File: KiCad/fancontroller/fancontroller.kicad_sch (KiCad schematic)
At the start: 17 parts, among them IC1 NE555DR, IC2 LM311DR, IC3 NE555DR, J1 Fan 4-pin, J2 Power input, P1 10k

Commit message: feat: save PCB reconstruction checkpoint and detailed passdown
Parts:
- added H1, H2, H3, H4: M2 mounting hole, MountingHole:MountingHole_2.2mm_M2, symbol Mechanical:MountingHole
- J1: footprint (none) -> Connector:FanPinHeader_1x04_P2.54mm_Vertical
- J2: footprint (none) -> Connector_PinHeader_2.54mm:PinHeader_1x02_P2.54mm_Vertical
- P1: footprint (none) -> Connector_PinHeader_2.54mm:PinHeader_1x03_P2.54mm_Vertical
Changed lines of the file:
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@@
 			(effects (font (size 1.27 1.27)))
 		)
-		(property "Footprint" ""
+		(property "Footprint" "Connector_PinHeader_2.54mm:PinHeader_1x03_P2.54mm_Vertical"
 			(at 124.46 100.33 0)
 			(effects (font (size 1.27 1.27)) (hide yes))
@@
 			(effects (font (size 1.27 1.27)))
 		)
-		(property "Footprint" ""
+		(property "Footprint" "Connector:FanPinHeader_1x04_P2.54mm_Vertical"
 			(at 265.43 64.77 0)
 			(effects (font (size 1.27 1.27)) (hide yes))
@@
 			(effects (font (size 1.27 1.27)))
 		)
-		(property "Footprint" ""
+		(property "Footprint" "Connector_PinHeader_2.54mm:PinHeader_1x02_P2.54mm_Vertical"
 			(at 265.43 115.57 0)
 			(effects (font (size 1.27 1.27)) (hide yes))
@@
 	(no_connect (at 144.78 77.47))
 	(no_connect (at 147.32 77.47))
+	(symbol
+		(lib_id "Mechanical:MountingHole")
+		(at 30.48 30.48 0)
+		(unit 1)
+		(exclude_from_sim no)
+		(in_bom yes)
+		(on_board yes)
+		(dnp no)
+		(property "Reference" "H1"
+			(at 30.48 26.67 0)
+			(effects (font (size 1.27 1.27)))
+		)
+		(property "Value" "M2 mounting hole"
+			(at 30.48 34.29 0)
+			(effects (font (size 1.27 1.27)))
+		)
+		(property "Footprint" "MountingHole:MountingHole_2.2mm_M2"
+			(at 30.48 30.48 0)
+			(effects (font (size 1.27 1.27)) (hide yes))
+		)
+		(property "Datasheet" "~"
+			(at 30.48 30.48 0)
+			(effects (font (size 1.27 1.27)) (hide yes))
+		)
+		(instances
+			(project "fancontroller"
+				(path "/97550efb-8a25-4e8f-a675-896628ec4139"
+					(reference "H1") (unit 1)
+				)
+			)
+		)
+	)
+	(symbol
+		(lib_id "Mechanical:MountingHole")
+		(at 50.8 30.48 0)
+		(unit 1)
+		(exclude_from_sim no)
+		(in_bom yes)
+		(on_board yes)
+		(dnp no)
+		(property "Reference" "H2"
+			(at 50.8 26.67 0)
+			(effects (font (size 1.27 1.27)))
+		)
+		(property "Value" "M2 mounting hole"
+			(at 50.8 34.29 0)
+			(effects (font (size 1.27 1.27)))
+		)
+		(property "Footprint" "MountingHole:MountingHole_2.2mm_M2"
+			(at 50.8 30.48 0)
+			(effects (font (size 1.27 1.27)) (hide yes))
+		)
+		(property "Datasheet" "~"
+			(at 50.8 30.48 0)
+			(effects (font (size 1.27 1.27)) (hide yes))
+		)
+		(instances
+			(project "fancontroller"
+				(path "/97550efb-8a25-4e8f-a675-896628ec4139"
+					(reference "H2") (unit 1)
+				)
+			)
+		)
+	)
+	(symbol
+		(lib_id "Mechanical:MountingHole")
+		(at 175.26 30.48 0)
+		(unit 1)
+		(exclude_from_sim no)
+		(in_bom yes)
+		(on_board yes)
+		(dnp no)
+		(property "Reference" "H3"
+			(at 175.26 26.67 0)
+			(effects (font (size 1.27 1.27)))
+		)
+		(property "Value" "M2 mounting hole"
+			(at 175.26 34.29 0)
+			(effects (font (size 1.27 1.27)))
+		)
+		(property "Footprint" "MountingHole:MountingHole_2.2mm_M2"
+			(at 175.26 30.48 0)
+			(effects (font (size 1.27 1.27)) (hide yes))
+		)
+		(property "Datasheet" "~"
+			(at 175.26 30.48 0)
+			(effects (font (size 1.27 1.27)) (hide yes))
+		)
+		(instances
+			(project "fancontroller"
+				(path "/97550efb-8a25-4e8f-a675-896628ec4139"
+					(reference "H3") (unit 1)
+				)
+			)
+		)
+	)
+	(symbol
+		(lib_id "Mechanical:MountingHole")
+		(at 195.58 30.48 0)
+		(unit 1)
+		(exclude_from_sim no)
+		(in_bom yes)
+		(on_board yes)
+		(dnp no)
+		(property "Reference" "H4"
+			(at 195.58 26.67 0)
+			(effects (font (size 1.27 1.27)))
+		)
+		(property "Value" "M2 mounting hole"
+			(at 195.58 34.29 0)
+			(effects (font (size 1.27 1.27)))
+		)
+		(property "Footprint" "MountingHole:MountingHole_2.2mm_M2"
+			(at 195.58 30.48 0)
+			(effects (font (size 1.27 1.27)) (hide yes))
+		)
+		(property "Datasheet" "~"
+			(at 195.58 30.48 0)
+			(effects (font (size 1.27 1.27)) (hide yes))
+		)
+		(instances
+			(project "fancontroller"
+				(path "/97550efb-8a25-4e8f-a675-896628ec4139"
+					(reference "H4") (unit 1)
+				)
+			)
+		)
+	)
 	(wire
 		(pts (xy 97.79 29.21) (xy 102.87 29.21))

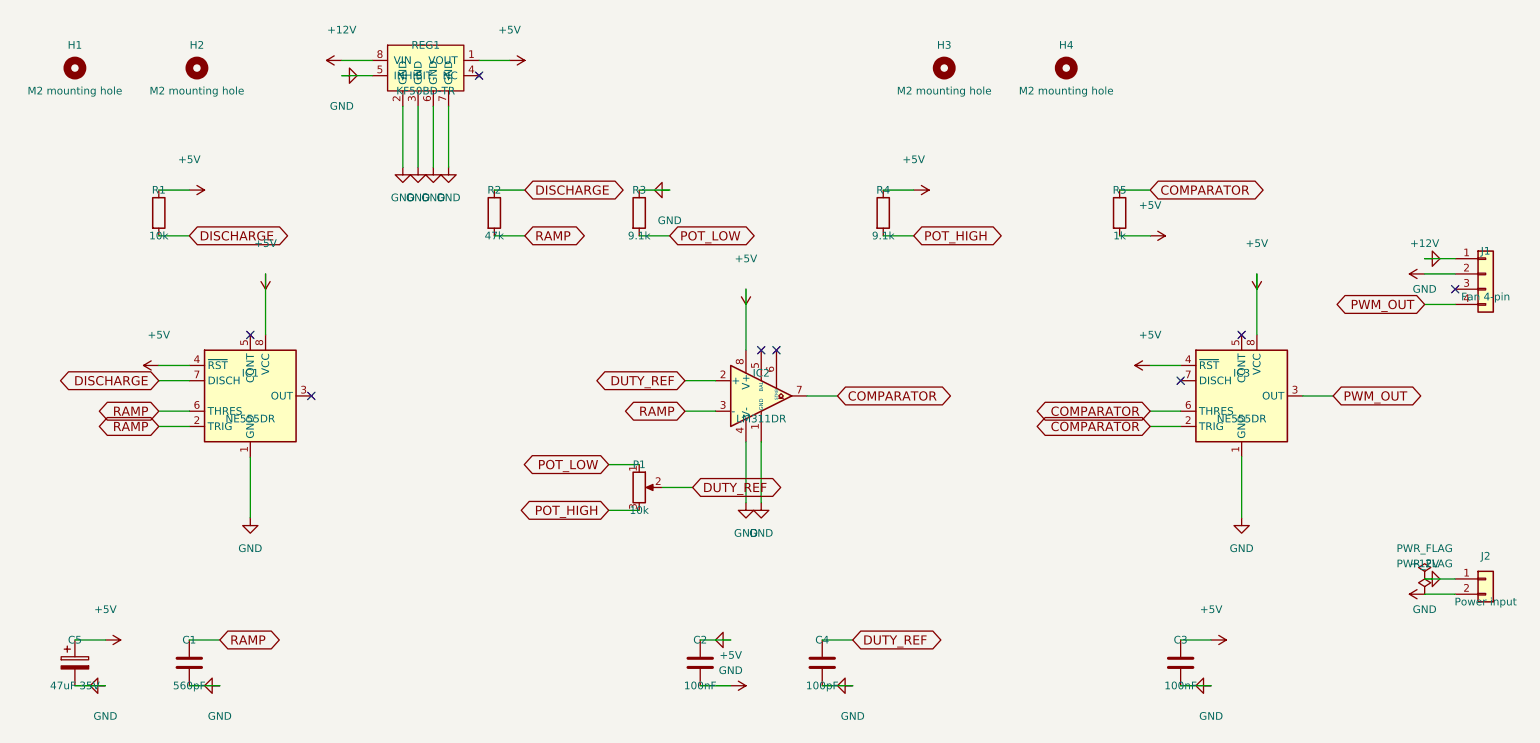
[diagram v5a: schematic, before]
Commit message: feat: clear native ERC and DRC and export revised 12 V assembly candidate
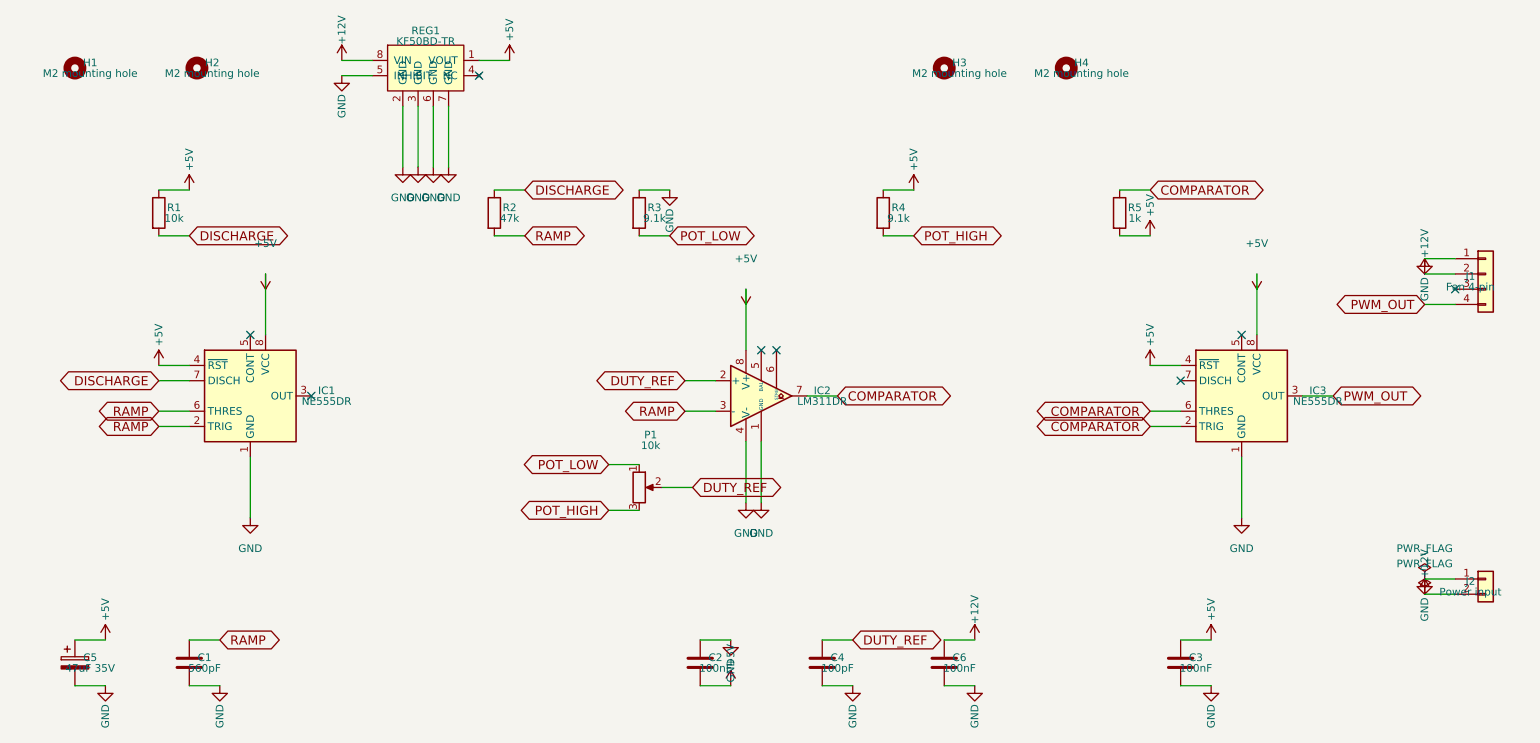
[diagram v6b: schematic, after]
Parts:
- added C6: 100nF, Recovered2018:C_0603_1608Metric_Pad1.05x0.95mm_HandSolder, symbol Device:C
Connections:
- net +12V: now also C6.1
- net GND: now also C6.2
